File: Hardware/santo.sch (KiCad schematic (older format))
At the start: 8 parts, among them J1 USB_C_Receptacle, J2 Audio-Jack-4, U1 ATMEGA32U4-MU

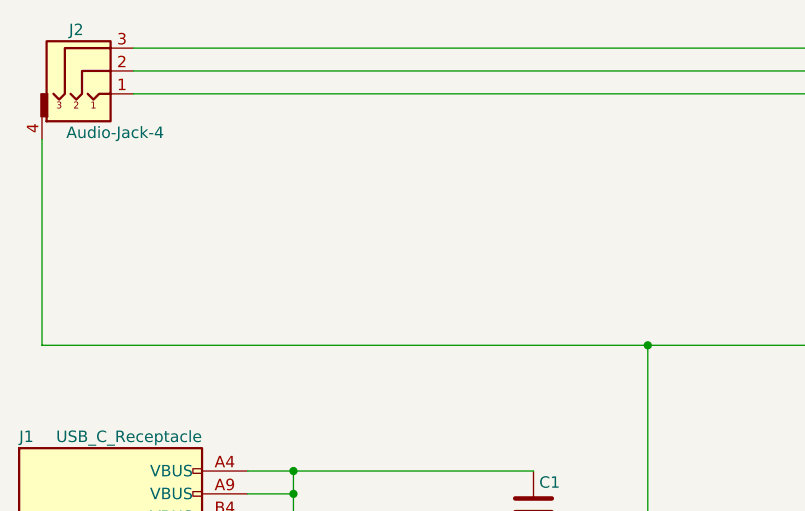
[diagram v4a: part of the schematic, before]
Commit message: Add pull up Rs
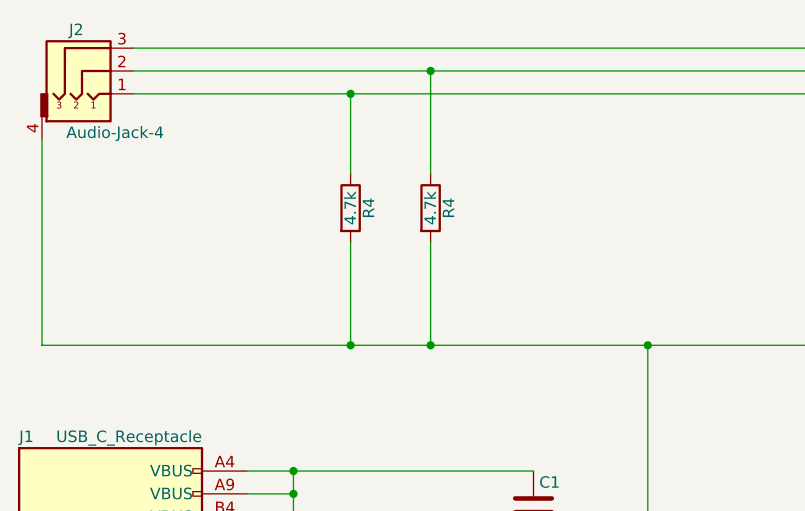
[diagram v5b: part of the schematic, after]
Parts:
- added R4 (x2): 4.7k, symbol R
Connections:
- net at C1.2, J2.4, U1.14 (VCC)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: now also R4.2, R4.2
- net at J2.1, U1.18 ((OC0B/SCL/INT0)PD0): now also R4.1
- net at J2.2, U1.19 ((SDA/INT1)PD1): now also R4.1
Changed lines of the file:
@@
 	9850 6600 9850 6950
 Connection ~ 9850 6950
+$Comp
+L R R4
+U 1 1 59F7D580
+P 6850 2350
+F 0 "R4" V 6930 2350 50  0000 C CNN
+F 1 "4.7k" V 6850 2350 50  0000 C CNN
+F 2 "" V 6780 2350 50  0001 C CNN
+F 3 "" H 6850 2350 50  0001 C CNN
+	1    6850 2350
+	1    0    0    -1
+$EndComp
+$Comp
+L R R4
+U 1 1 59F7D5AF
+P 6500 2350
+F 0 "R4" V 6580 2350 50  0000 C CNN
+F 1 "4.7k" V 6500 2350 50  0000 C CNN
+F 2 "" V 6430 2350 50  0001 C CNN
+F 3 "" H 6500 2350 50  0001 C CNN
+	1    6500 2350
+	1    0    0    -1
+$EndComp
+Wire Wire Line
+	6500 2200 6500 1850
+Connection ~ 6500 1850
+Wire Wire Line
+	6500 2500 6500 2950
+Connection ~ 6500 2950
+Wire Wire Line
+	6850 1750 6850 2200
+Connection ~ 6850 1750
+Wire Wire Line
+	6850 2500 6850 2950
+Connection ~ 6850 2950
 $EndSCHEMATC

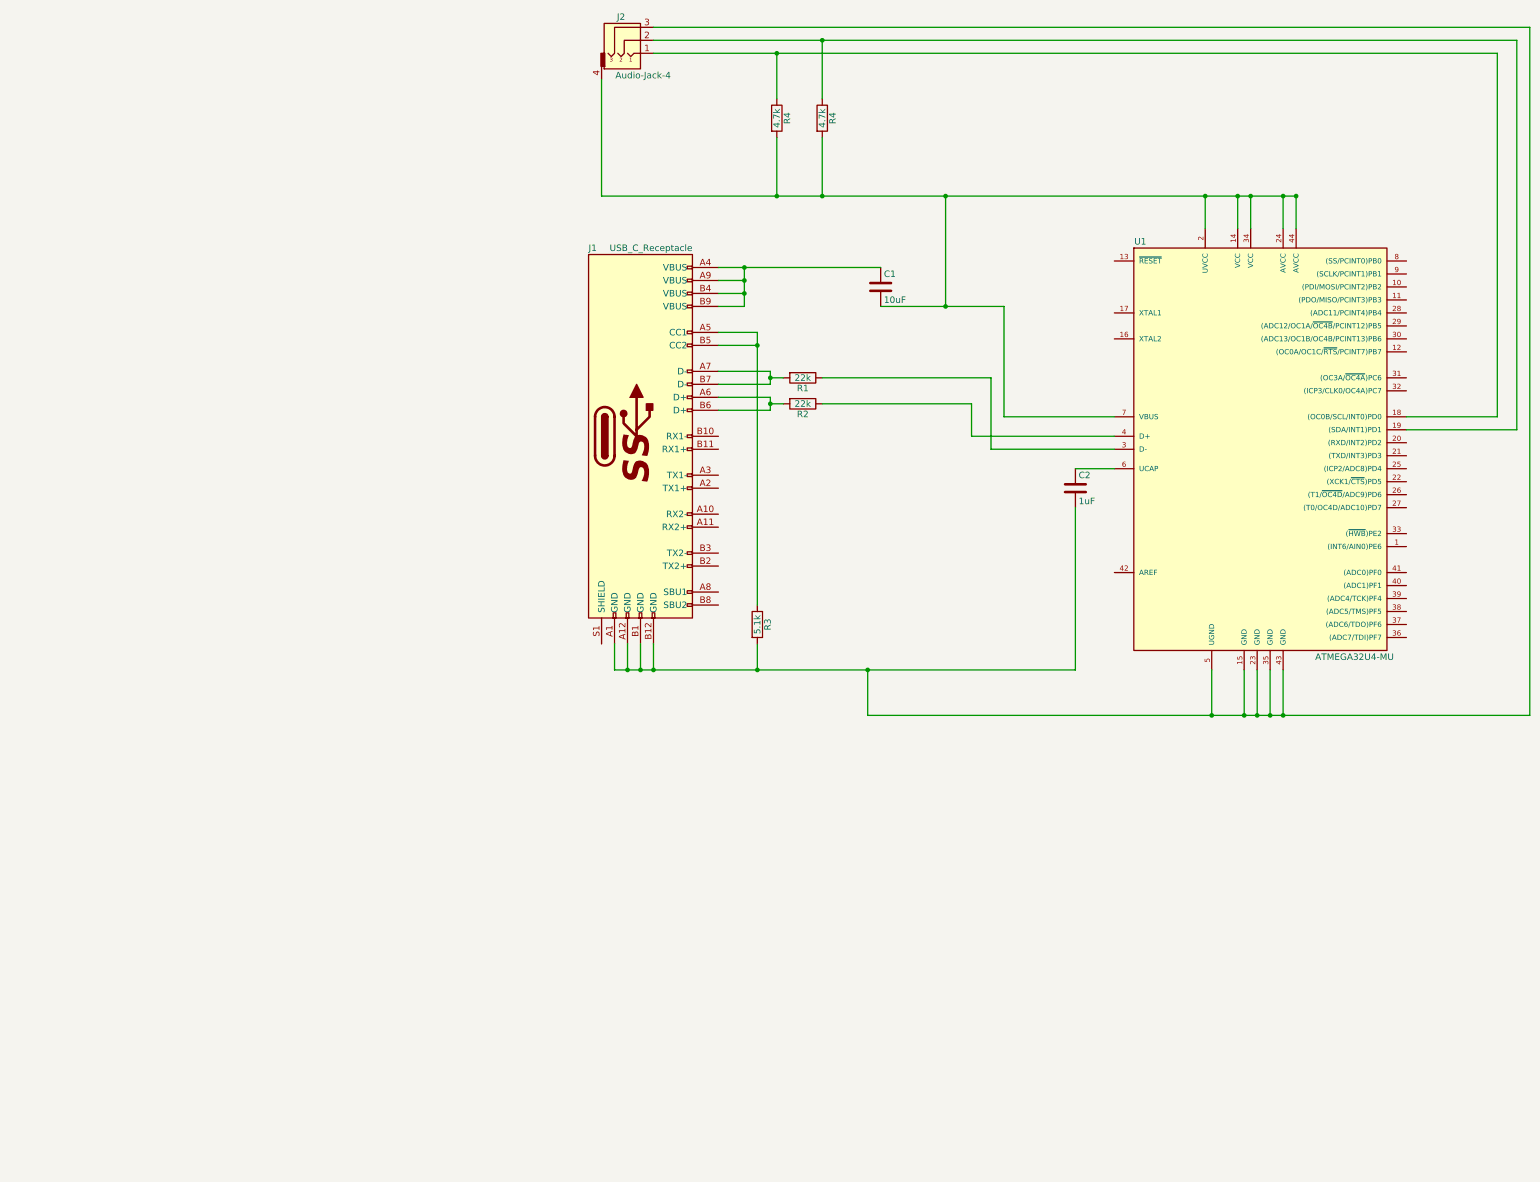
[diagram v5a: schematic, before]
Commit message: Change from RTTS to USB-C for inter board communication over I2C
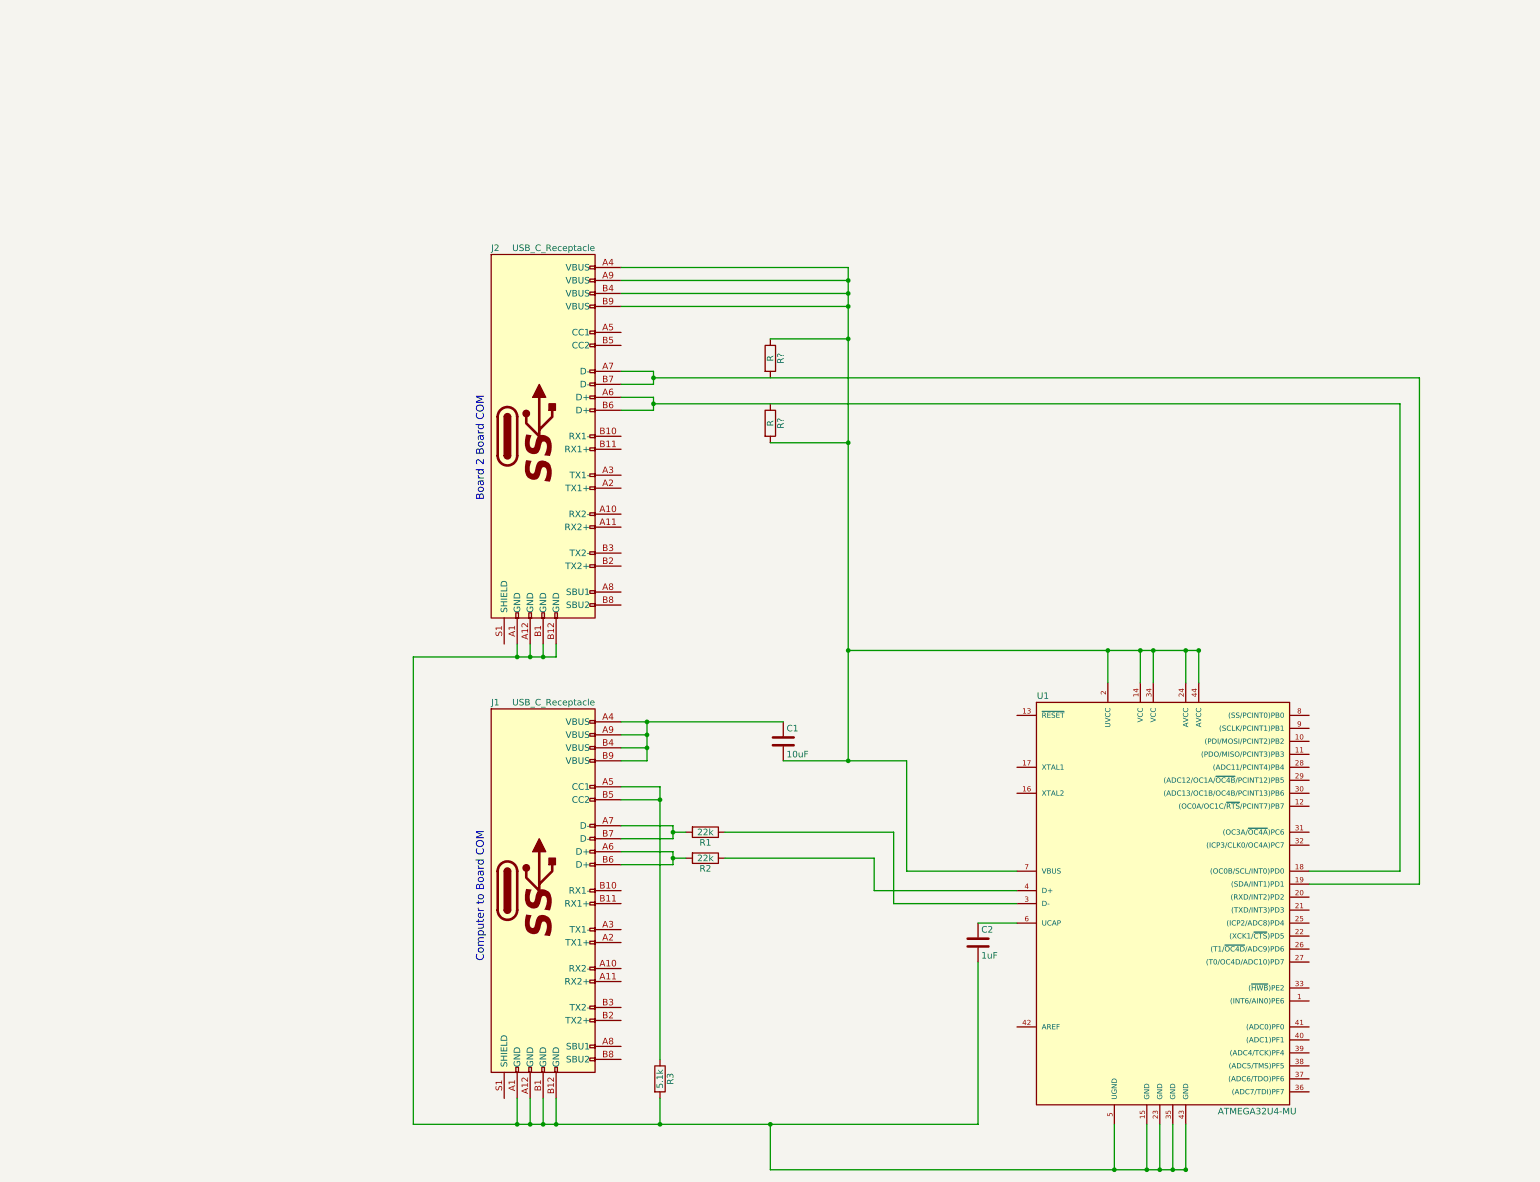
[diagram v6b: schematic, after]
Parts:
- removed J2: Audio-Jack-4, symbol Audio-Jack-4
- removed R4 (x2): 4.7k, symbol R
- added J2: USB_C_Receptacle, symbol USB_C_Receptacle
- added R? (x2): R, symbol R
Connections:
- net at C2.2, J1.A1 (GND), J1.A12 (GND)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: now also J2.A1 (GND), J2.A12 (GND), J2.B1 (GND), J2.B12 (GND)
- net at C1.2, U1.14 (VCC), U1.2 (UVCC)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: now also J2.A4 (VBUS), J2.A9 (VBUS), J2.B4 (VBUS), J2.B9 (VBUS), R?.1, R?.2
- net at U1.18 ((OC0B/SCL/INT0)PD0): now also J2.A6 (D+), J2.B6 (D+)
- net at U1.19 ((SDA/INT1)PD1): now also J2.A7 (D-), J2.B7 (D-)
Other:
- note added: "Board 2 Board COM"
- note added: "Computer to Board COM"
- moved on the sheet: C1, C2, J1, R1, R2, R3, U1

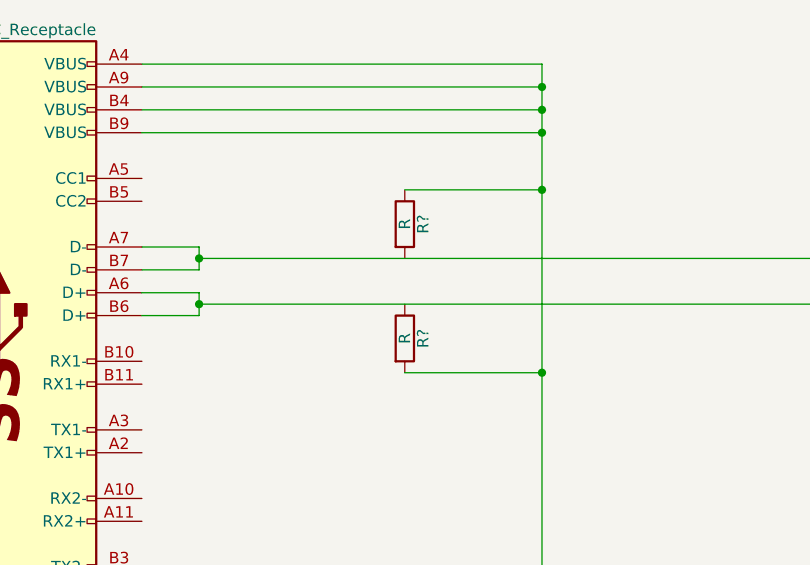
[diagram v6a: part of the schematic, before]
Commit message: Add the resistor value for the pull us on the I2C bus.
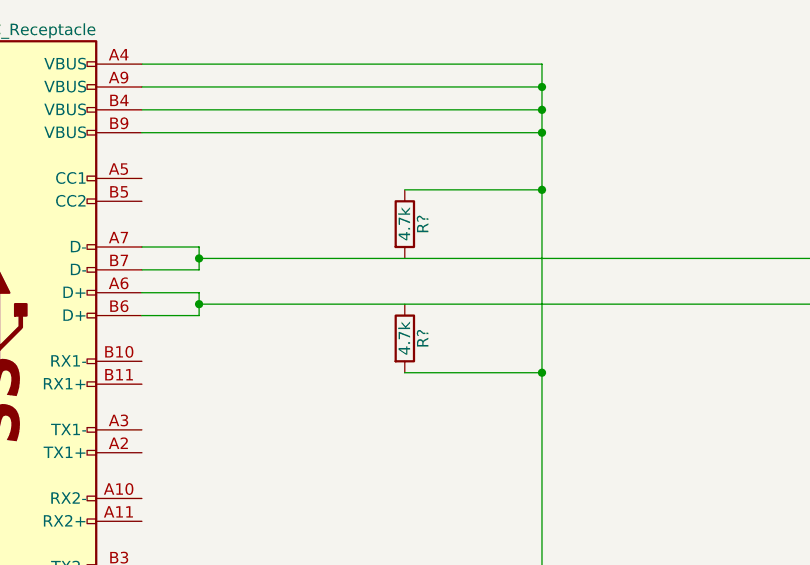
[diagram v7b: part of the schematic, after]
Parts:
- R? (x2): value R -> 4.7k
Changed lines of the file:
@@
 P 6450 4700
 F 0 "R?" V 6530 4700 50  0000 C CNN
-F 1 "R" V 6450 4700 50  0000 C CNN
+F 1 "4.7k" V 6450 4700 50  0000 C CNN
 F 2 "" V 6380 4700 50  0001 C CNN
 F 3 "" H 6450 4700 50  0001 C CNN
@@
 P 6450 4200
 F 0 "R?" V 6530 4200 50  0000 C CNN
-F 1 "R" V 6450 4200 50  0000 C CNN
+F 1 "4.7k" V 6450 4200 50  0000 C CNN
 F 2 "" V 6380 4200 50  0001 C CNN
 F 3 "" H 6450 4200 50  0001 C CNN
